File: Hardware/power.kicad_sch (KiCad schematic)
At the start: 24 parts, among them J3 Conn_01x02_Pin, J4 USB4105-GF-A, Q1 DMG3415UFY4Q-7, U1 AP7361C-33E, U5 MCP73831-2-OT

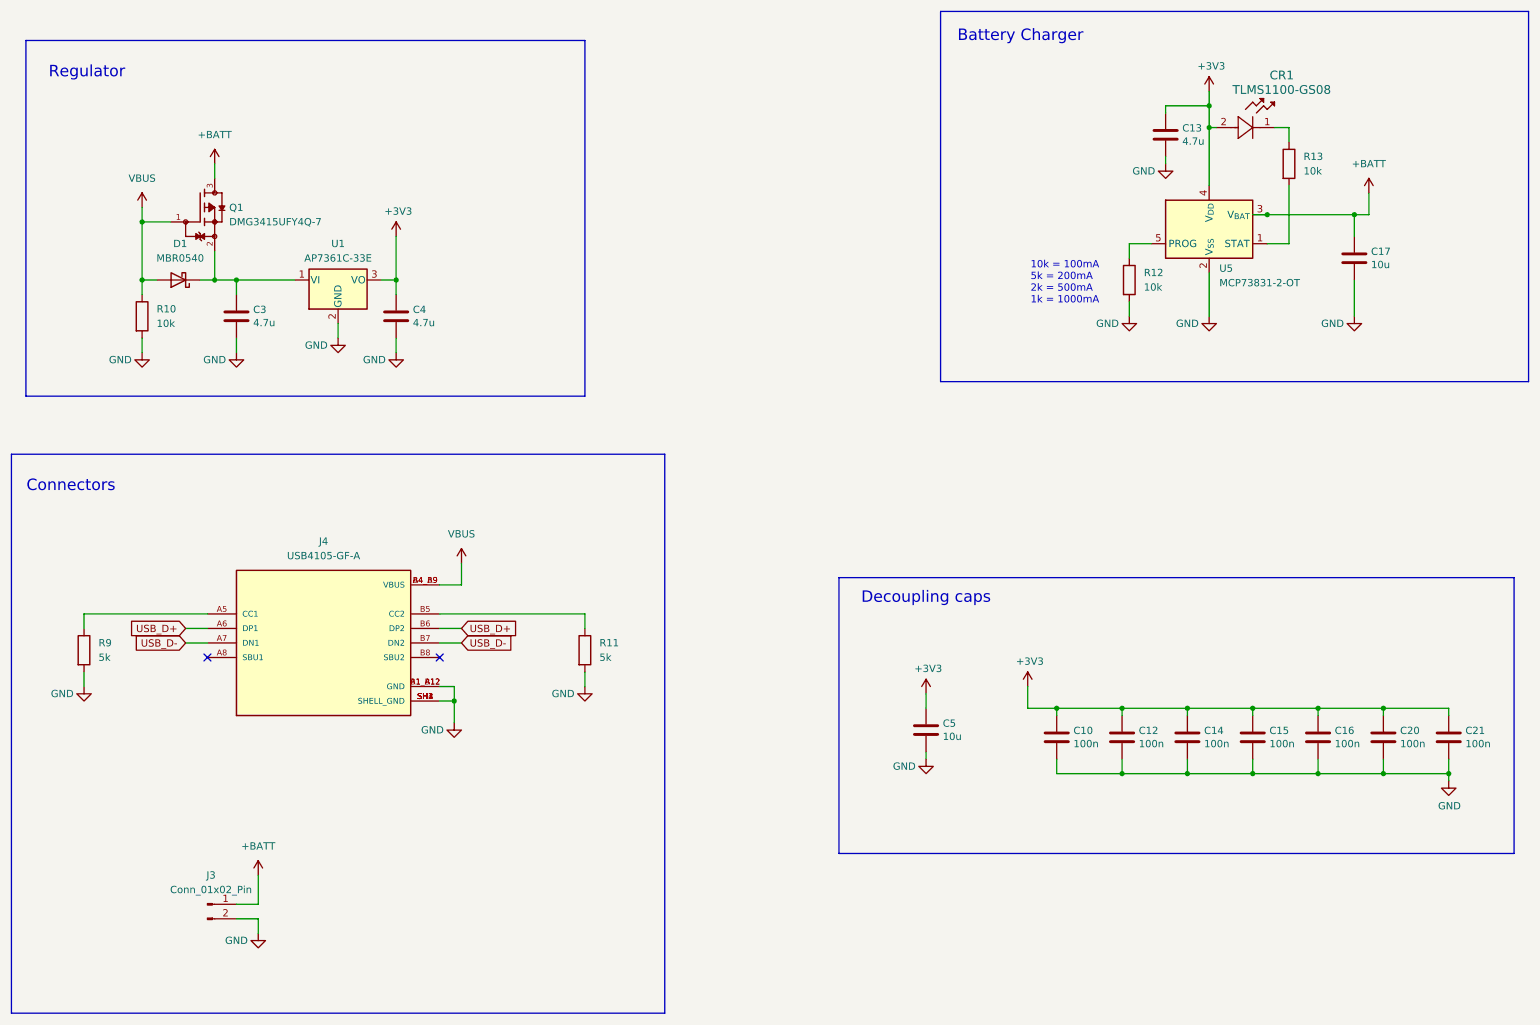
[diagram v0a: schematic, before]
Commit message: Added new components to sch and pcb and redid the routing and layout of pcb
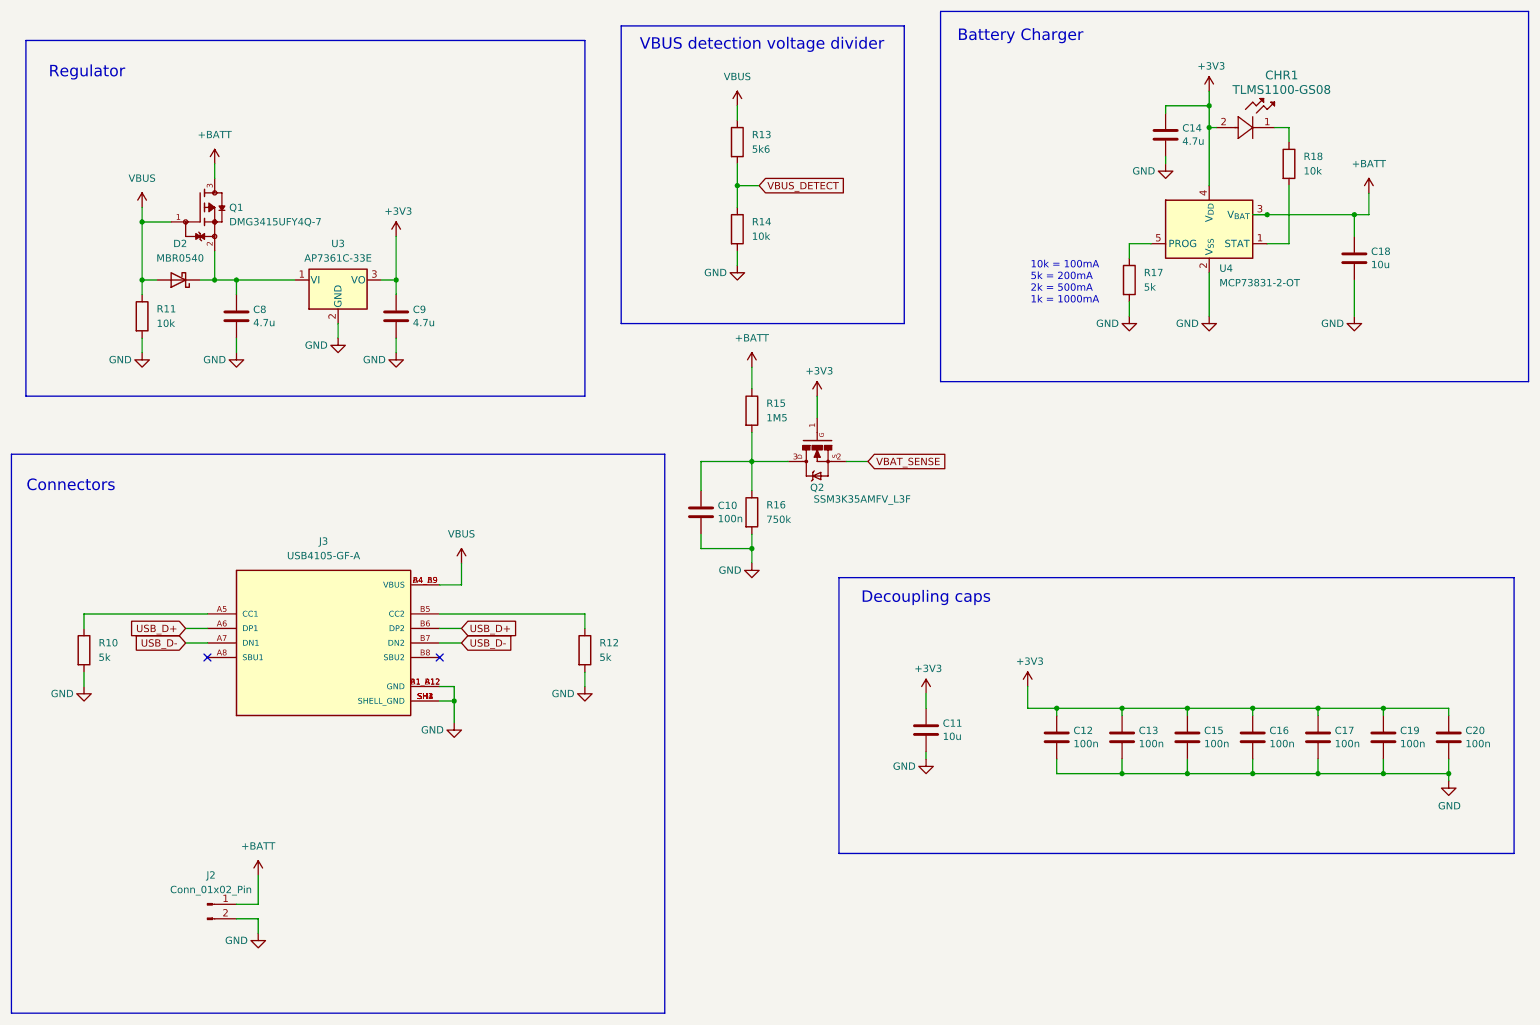
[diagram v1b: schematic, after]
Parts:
- added C10: 100n, Capacitor_SMD:C_0402_1005Metric, symbol Device:C
- added Q2: SSM3K35AMFV_L3F, duso:VESM_SOT-723_, symbol SSM3K35AMFV_L3F:SSM3K35AMFV_L3F
- added R13: 5k6, Resistor_SMD:R_0402_1005Metric, symbol Device:R
- added R14: 10k, Resistor_SMD:R_0402_1005Metric, symbol Device:R
- added R15: 1M5, Resistor_SMD:R_0402_1005Metric, symbol Device:R
- added R16: 750k, Resistor_SMD:R_0402_1005Metric, symbol Device:R
- R10: renamed from R9; footprint Resistor_SMD:R_0603_1608Metric -> Resistor_SMD:R_0402_1005Metric
- R11: renamed from R10; footprint Resistor_SMD:R_0603_1608Metric -> Resistor_SMD:R_0402_1005Metric
- R12: renamed from R11; footprint Resistor_SMD:R_0603_1608Metric -> Resistor_SMD:R_0402_1005Metric
- R17: renamed from R12; value 10k -> 5k; footprint Resistor_SMD:R_0603_1608Metric -> Resistor_SMD:R_0402_1005Metric
- R18: renamed from R13; footprint Resistor_SMD:R_0603_1608Metric -> Resistor_SMD:R_0402_1005Metric
- renumbered C5 to C11, C10 to C12, C12 to C13, C13 to C14, C14 to C15, C15 to C16, C16 to C17, C17 to C18, C20 to C19, C21 to C20, C3 to C8, C4 to C9, CR1 to CHR1, D1 to D2, J3 to J2, J4 to J3, U1 to U3, U5 to U4
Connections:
- net +3V3: now also Q2.1
- net +BATT: now also R15.1
- net GND: now also C10.2, R14.2, R16.2
- net VBUS: now also R13.1
- new net: C10.1, Q2.3, R15.2, R16.1
- new net VBAT_SENSE: Q2.2
- new net VBUS_DETECT: R13.2, R14.1
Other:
- note added: "VBUS detection voltage divider"

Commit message: Added external batt switch pin and bypass 0ohm res, changed ldo for smaller 600mA
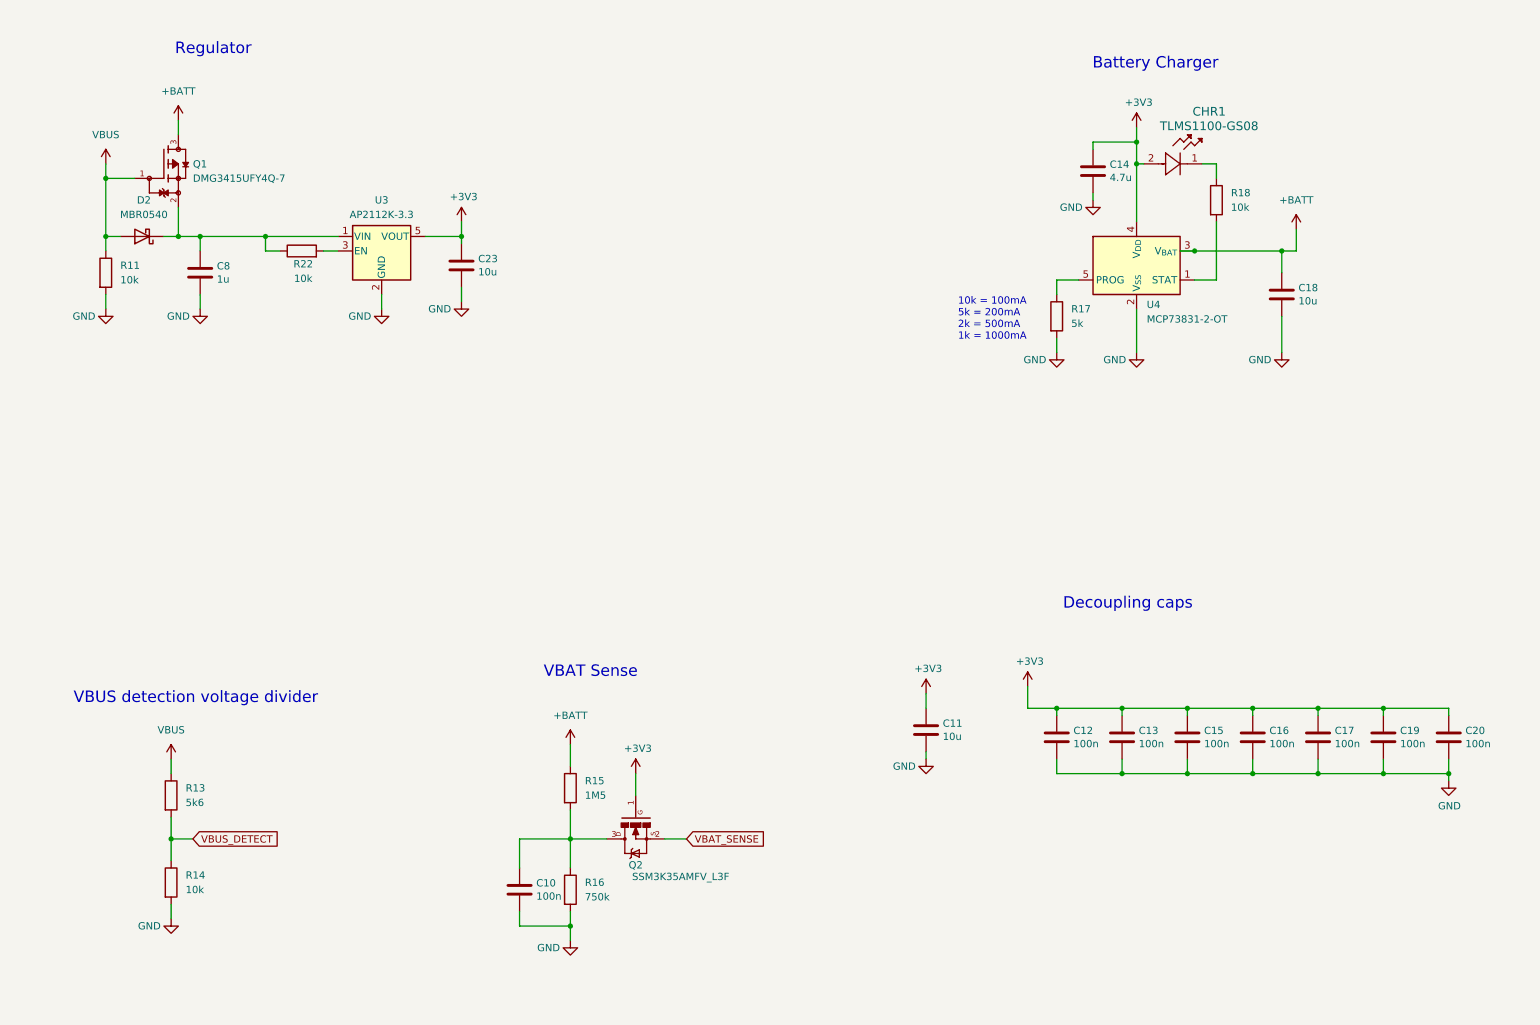
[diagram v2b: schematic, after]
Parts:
- removed C9: 4.7u, Capacitor_SMD:C_0402_1005Metric, symbol Device:C
- removed J2: Conn_01x02_Pin, Connector_JST:JST_PH_B2B-PH-K_1x02_P2.00mm_Vertical, symbol Connector:Conn_01x02_Pin
- removed J3: USB4105-GF-A, duso:GCT_USB4105-GF-A, symbol USB4105-GF-A:USB4105-GF-A
- removed R10, R12: 5k, Resistor_SMD:R_0402_1005Metric, symbol Device:R
- removed U3: AP7361C-33E, Package_TO_SOT_SMD:SOT-223-3_TabPin2, symbol Regulator_Linear:AP7361C-33E
- added C23: 10u, Capacitor_SMD:C_0402_1005Metric, symbol Device:C
- added R22: 10k, Resistor_SMD:R_0402_1005Metric, symbol Device:R
- added U3: AP2112K-3.3, Package_TO_SOT_SMD:SOT-23-5, symbol Regulator_Linear:AP2112K-3.3
- C8: value 4.7u -> 1u
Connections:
- net +3V3: now also C23.1, U3.5 (VOUT)
- net GND: now also C23.2, U3.2 (GND)
- net at C8.1, D2.1 (K), Q1.2: now also R22.1, U3.1 (VIN)
- new net: R22.2, U3.3 (EN)
- no-connect marks 2 -> 0
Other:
- note added: "VBAT Sense"
- note removed: "Connectors"
- moved on the sheet: C10, C14, C18, C8, CHR1, D2, Q1, Q2, R11, R13, R14, R15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

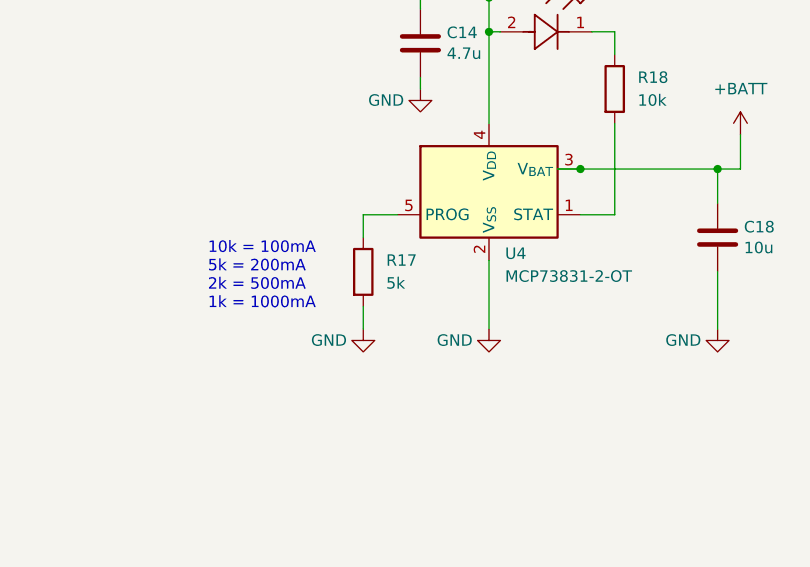
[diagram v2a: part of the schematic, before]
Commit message: Changed bat charge current to 100mA
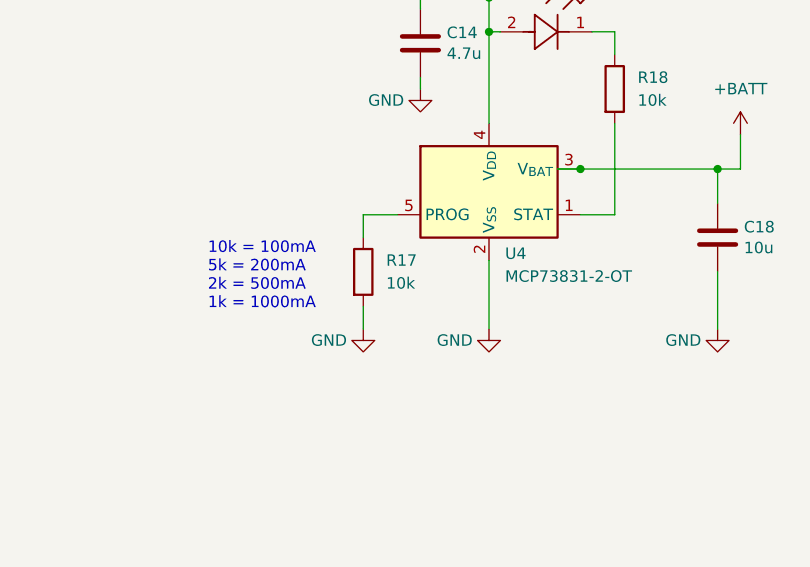
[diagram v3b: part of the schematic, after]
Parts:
- R17: value 5k -> 10k
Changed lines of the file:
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@@
 			)
 		)
-		(property "Value" "5k"
+		(property "Value" "10k"
 			(at 200.66 68.5799 0)
 			(effects
